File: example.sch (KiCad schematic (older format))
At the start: 14 parts, among them P1 CONN_01X03, P3 CONN_01X06, P4 CONN_01X01, P6 CONN_01X12, P7 CONN_01X16, P8 CONN_01X09

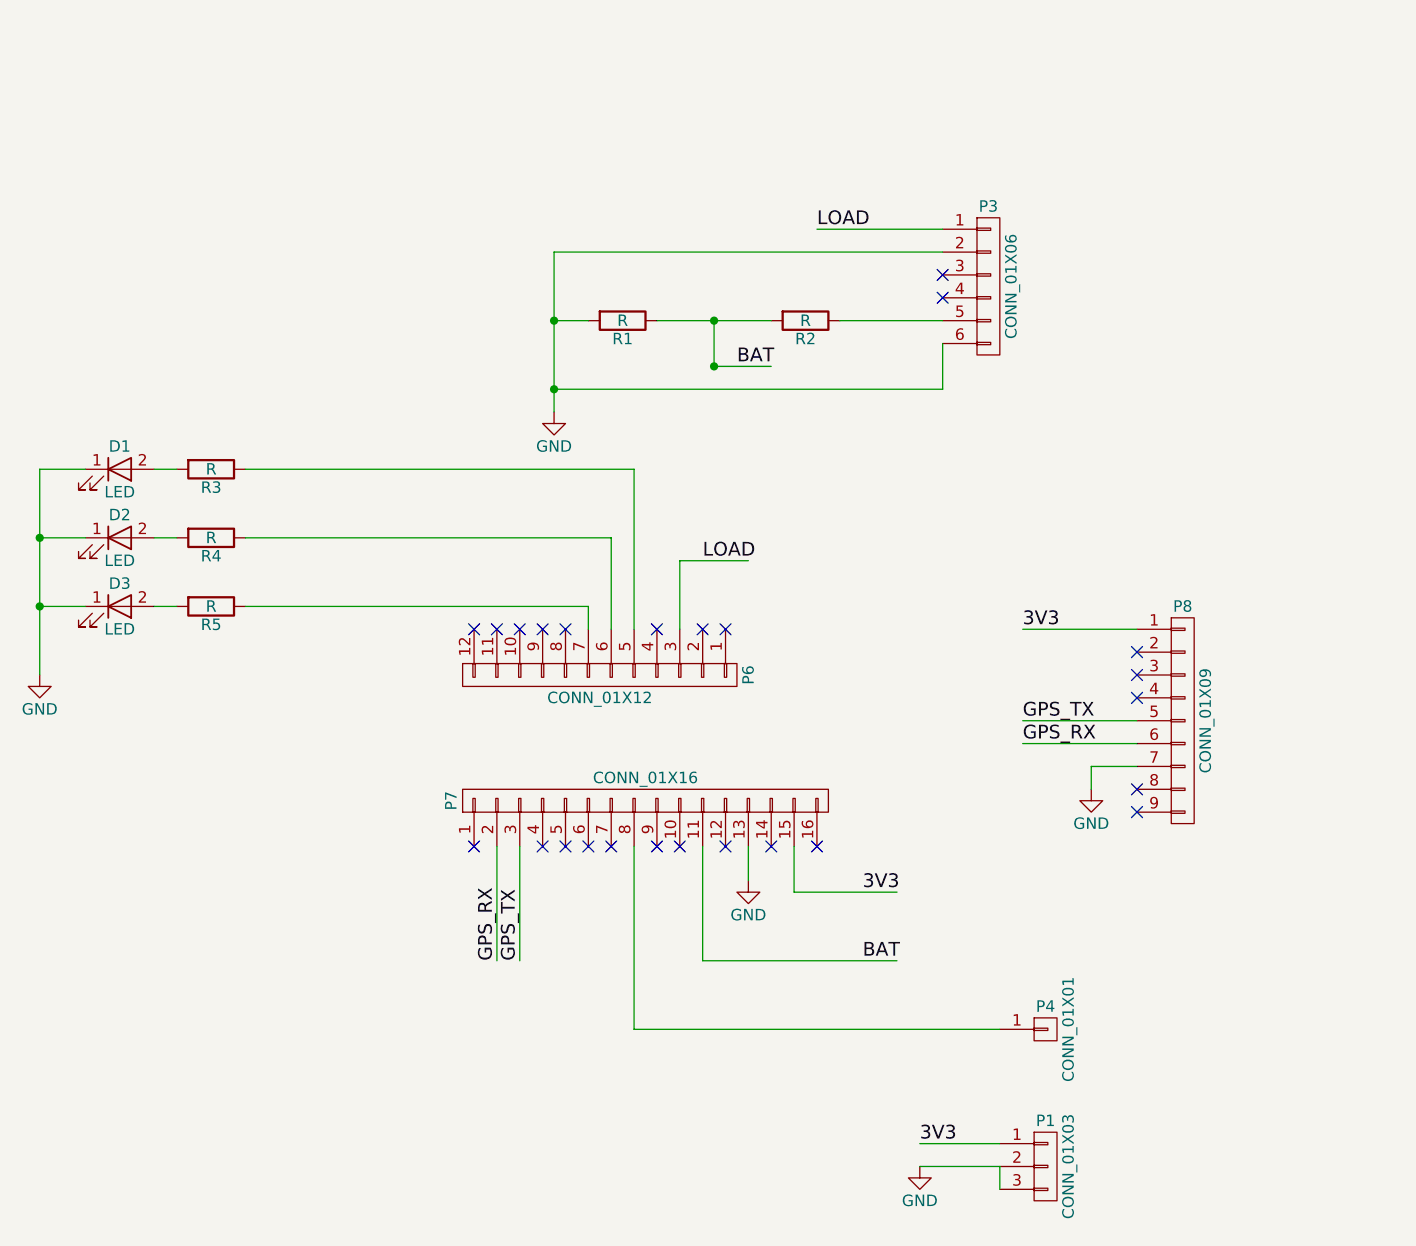
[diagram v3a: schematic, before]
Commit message: Drop the charging board, it's unnecessary. Make sensor a legit conn.
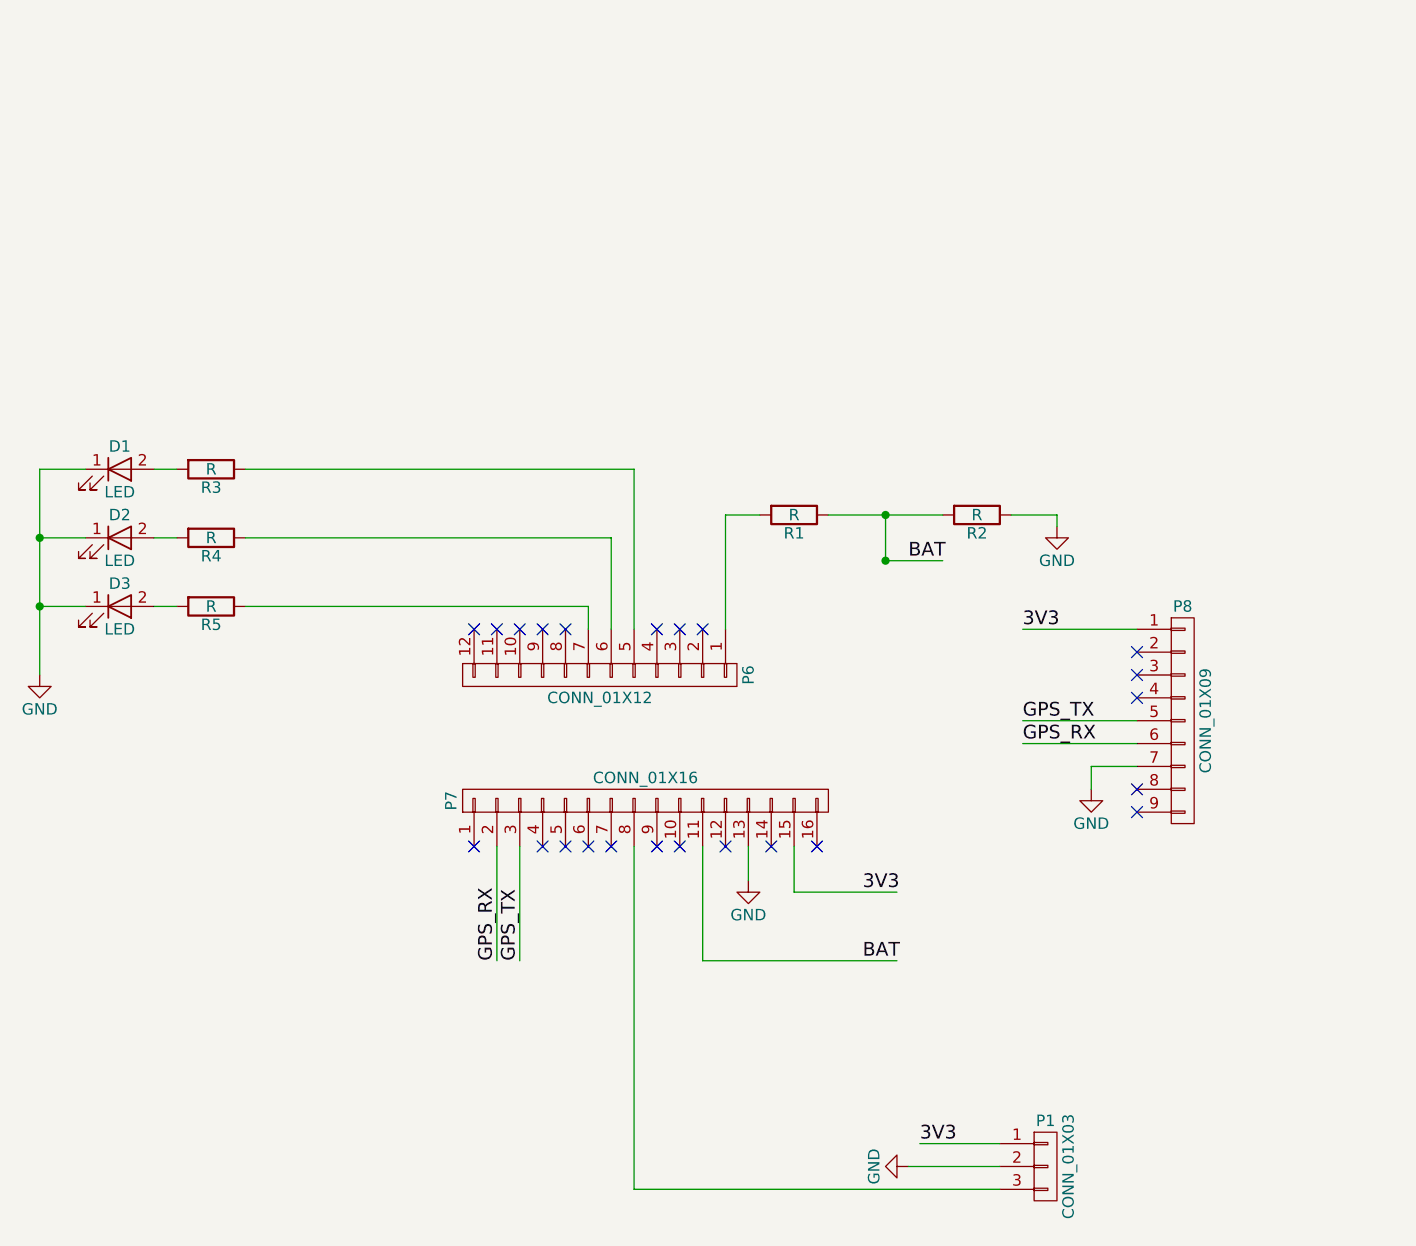
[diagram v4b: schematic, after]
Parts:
- removed P3: CONN_01X06, Socket_Strips:Socket_Strip_Straight_1x06, symbol CONN_01X06
- removed P4: CONN_01X01, Socket_Strips:Socket_Strip_Straight_1x01, symbol CONN_01X01
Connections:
- net labels removed: LOAD
- wire segments 42 -> 36
- no-connect marks 25 -> 23
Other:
- moved on the sheet: R1, R2
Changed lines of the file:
@@
 $EndDescr
-$Comp
-L CONN_01X06 P3
-U 1 1 5875956A
-P 5050 2400
-F 0 "P3" H 5050 2750 50  0000 C CNN
-F 1 "CONN_01X06" V 5150 2400 50  0000 C CNN
-F 2 "Socket_Strips:Socket_Strip_Straight_1x06" H 5050 2400 50  0001 C CNN
-F 3 "" H 5050 2400 50  0000 C CNN
-	1    5050 2400
-	1    0    0    -1
-$EndComp
 $Comp
 L R R1
 U 1 1 587596E9
-P 3450 2550
-F 0 "R1" V 3530 2550 50  0000 C CNN
-F 1 "R" V 3450 2550 50  0000 C CNN
-F 2 "Resistors_THT:Resistor_Horizontal_RM7mm" V 3380 2550 50  0001 C CNN
-F 3 "" H 3450 2550 50  0000 C CNN
-	1    3450 2550
+P 4200 3400
+F 0 "R1" V 4280 3400 50  0000 C CNN
+F 1 "R" V 4200 3400 50  0000 C CNN
+F 2 "Resistors_THT:Resistor_Horizontal_RM7mm" V 4130 3400 50  0001 C CNN
+F 3 "" H 4200 3400 50  0000 C CNN
+	1    4200 3400
 	0    1    1    0
 $EndComp
@@
 L R R2
 U 1 1 58759766
-P 4250 2550
-F 0 "R2" V 4330 2550 50  0000 C CNN
-F 1 "R" V 4250 2550 50  0000 C CNN
-F 2 "Resistors_THT:Resistor_Horizontal_RM7mm" V 4180 2550 50  0001 C CNN
-F 3 "" H 4250 2550 50  0000 C CNN
-	1    4250 2550
-	0    1    1    0
-$EndComp
-$Comp
-L GND #PWR01
-U 1 1 58759956
-P 3150 2950
-F 0 "#PWR01" H 3150 2700 50  0001 C CNN
-F 1 "GND" H 3150 2800 50  0000 C CNN
-F 2 "" H 3150 2950 50  0000 C CNN
-F 3 "" H 3150 2950 50  0000 C CNN
-	1    3150 2950
-	1    0    0    -1
-$EndComp
-NoConn ~ 4850 2450
-NoConn ~ 4850 2350
-$Comp
-L CONN_01X12 P6
-U 1 1 58764702
-P 3350 4100
-F 0 "P6" H 3350 4750 50  0000 C CNN
-F 1 "CONN_01X12" V 3450 4100 50  0000 C CNN
-F 2 "Socket_Strips:Socket_Strip_Straight_1x12" H 3350 4100 50  0001 C CNN
-F 3 "" H 3350 4100 50  0000 C CNN
-	1    3350 4100
+P 5000 3400
+F 0 "R2" V 5080 3400 50  0000 C CNN
+F 1 "R" V 5000 3400 50  0000 C CNN
+F 2 "Resistors_THT:Resistor_Horizontal_RM7mm" V 4930 3400 50  0001 C CNN
+F 3 "" H 5000 3400 50  0000 C CNN
+	1    5000 3400
 	0    1    1    0
 $EndComp
@@
 	1    0    0    -1
 $EndComp
-Text Label 3950 2750 0    60   ~ 0
+Text Label 4700 3600 0    60   ~ 0
 BAT
-Text Label 4300 2150 0    60   ~ 0
-LOAD
-Text Label 3800 3600 0    60   ~ 0
-LOAD
 $Comp
 L GND #PWR03
@@
 GPS_RX
 NoConn ~ 3800 3900
-NoConn ~ 3900 3900
 Text Label 4750 6150 0    60   ~ 0
 3V3
@@
 L GND #PWR04
 U 1 1 58768B90
-P 4750 6250
-F 0 "#PWR04" H 4750 6000 50  0001 C CNN
-F 1 "GND" H 4750 6100 50  0000 C CNN
-F 2 "" H 4750 6250 50  0000 C CNN
-F 3 "" H 4750 6250 50  0000 C CNN
-	1    4750 6250
-	1    0    0    -1
-$EndComp
-$Comp
-L CONN_01X01 P4
-U 1 1 58768E8C
-P 5300 5650
-F 0 "P4" H 5300 5750 50  0000 C CNN
-F 1 "CONN_01X01" V 5400 5650 50  0000 C CNN
-F 2 "Socket_Strips:Socket_Strip_Straight_1x01" H 5300 5650 50  0001 C CNN
-F 3 "" H 5300 5650 50  0000 C CNN
-	1    5300 5650
-	1    0    0    -1
+P 4700 6250
+F 0 "#PWR04" H 4700 6000 50  0001 C CNN
+F 1 "GND" H 4700 6100 50  0000 C CNN
+F 2 "" H 4700 6250 50  0000 C CNN
+F 3 "" H 4700 6250 50  0000 C CNN
+	1    4700 6250
+	0    1    1    0
 $EndComp
 $Comp
@@
 $EndComp
 Wire Wire Line
-	3600 2550 4100 2550
-Wire Wire Line
-	4850 2250 3150 2250
-Connection ~ 3150 2550
-Wire Wire Line
-	3850 2550 3850 2750
-Connection ~ 3850 2550
+	4350 3400 4850 3400
+Wire Wire Line
+	4600 3400 4600 3600
+Connection ~ 4600 3400
 Wire Wire Line
 	5500 4600 5500 4500
 Wire Wire Line
 	5500 4500 5700 4500
-Connection ~ 3850 2750
-Wire Wire Line
-	4850 2150 4300 2150
-Wire Wire Line
-	3700 3900 3700 3600
-Wire Wire Line
-	3700 3600 4000 3600
+Connection ~ 4600 3600
 Wire Wire Line
 	4000 5000 4000 4850
@@
 	2900 4850 2900 5350
 Wire Wire Line
-	3500 4850 3500 5650
-Wire Wire Line
-	3500 5650 5100 5650
-Wire Wire Line
-	3850 2750 4100 2750
+	4600 3600 4850 3600
 Wire Wire Line
 	5100 6150 4750 6150
 Wire Wire Line
-	5100 6250 4750 6250
-Wire Wire Line
-	5100 6350 5100 6250
+	4700 6250 5100 6250
 Wire Wire Line
 	5700 4300 5200 4300
 Wire Wire Line
 	5700 4400 5200 4400
-Wire Wire Line
-	4850 2550 4400 2550
-Wire Wire Line
-	3300 2550 3150 2550
-Wire Wire Line
-	3150 2250 3150 2950
-Wire Wire Line
-	4850 2650 4850 2850
-Wire Wire Line
-	4850 2850 3150 2850
-Connection ~ 3150 2850
 Wire Wire Line
 	900  3200 900  4100
@@
 Wire Wire Line
 	3500 3200 1800 3200
+NoConn ~ 3700 3900
+$Comp
+L CONN_01X12 P6
+U 1 1 58764702
+P 3350 4100
+F 0 "P6" H 3350 4750 50  0000 C CNN
+F 1 "CONN_01X12" V 3450 4100 50  0000 C CNN
+F 2 "Socket_Strips:Socket_Strip_Straight_1x12" H 3350 4100 50  0001 C CNN
+F 3 "" H 3350 4100 50  0000 C CNN
+	1    3350 4100
+	0    1    1    0
+$EndComp
+$Comp
+L GND #PWR?
+U 1 1 58DEADA2
+P 5350 3450
+F 0 "#PWR?" H 5350 3200 50  0001 C CNN
+F 1 "GND" H 5350 3300 50  0000 C CNN
+F 2 "" H 5350 3450 50  0000 C CNN
+F 3 "" H 5350 3450 50  0000 C CNN
+	1    5350 3450
+	1    0    0    -1
+$EndComp
+Wire Wire Line
+	5350 3450 5350 3400
+Wire Wire Line
+	5350 3400 5150 3400
+Wire Wire Line
+	3900 3900 3900 3400
+Wire Wire Line
+	3900 3400 4050 3400
+Wire Wire Line
+	3500 6350 5100 6350
+Wire Wire Line
+	3500 4850 3500 6350
 $EndSCHEMATC
